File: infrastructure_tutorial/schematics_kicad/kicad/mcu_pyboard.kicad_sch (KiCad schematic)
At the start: 0 parts

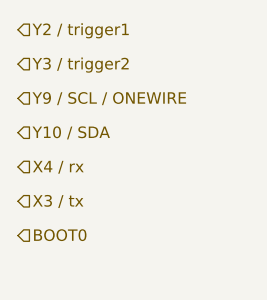
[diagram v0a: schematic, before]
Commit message: Connect pyboard/pico to ground
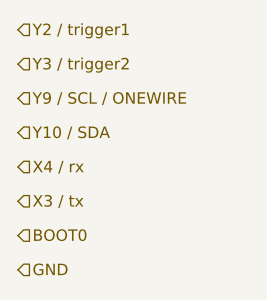
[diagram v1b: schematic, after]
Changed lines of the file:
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@@
+		)
+	)
+	(hierarchical_label "GND"
+		(shape input)
+		(at 69.85 77.47 0)
+		(fields_autoplaced yes)
+		(effects
+			(font
+				(size 1.27 1.27)
+			)
+			(justify left)
 		)
 	)
